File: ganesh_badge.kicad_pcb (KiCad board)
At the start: 2 copper layers, 36 x 47.8 mm, 14 parts, among them J1 Conn_01x03_Male, J2 USB_B_Micro, SW1 SW_Push, U1 ATtiny9-TS

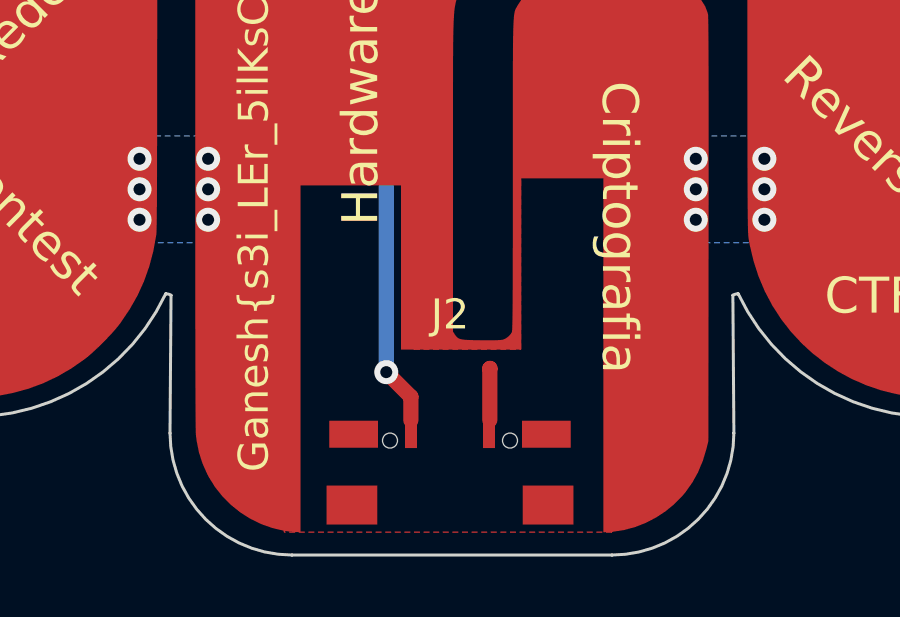
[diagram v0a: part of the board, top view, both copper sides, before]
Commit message: simple text fixes
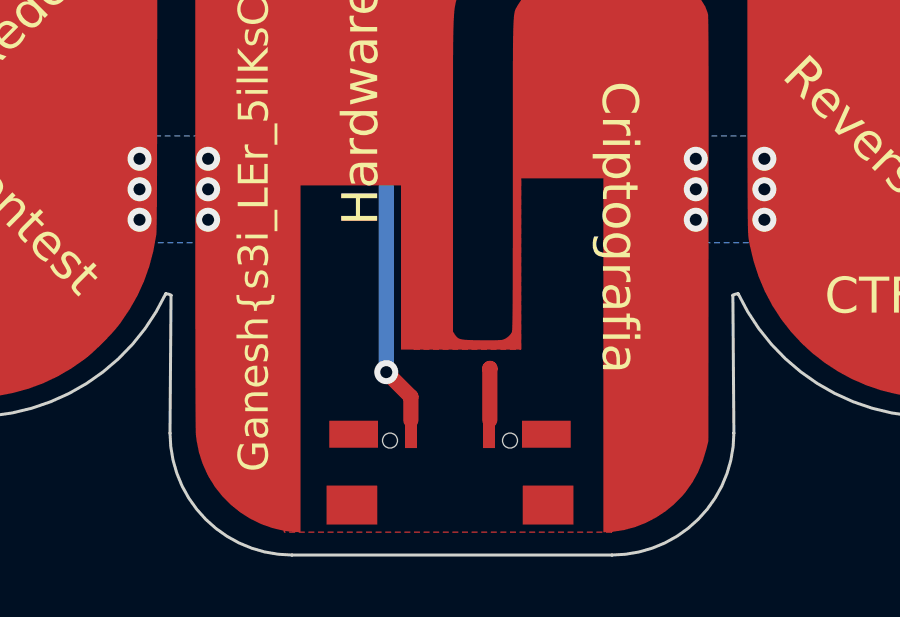
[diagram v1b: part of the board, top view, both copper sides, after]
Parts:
- C2: value 1.5 n -> 1.5 nF
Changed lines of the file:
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@@
     (property "Sheetname" "")
     (attr smd)
-    (fp_text reference "J2" (at 0 -7 unlocked) (layer "F.SilkS")
+    (fp_text reference "J2" (at 0 -7 unlocked) (layer "F.SilkS") hide
       (effects (font (size 1 1) (thickness 0.15)))
     )
@@
       (effects (font (size 1 1) (thickness 0.15)))
     )
-    (fp_text value "1.5 n" (at 2.084 0 180) (layer "F.Fab")
-      (effects (font (size 1 1) (thickness 0.15)))
-    )
+    (fp_text value "1.5 nF" (at 2.084 0 180) (layer "F.Fab")
+      (effects (font (size 1 1) (thickness 0.15)))
+    )

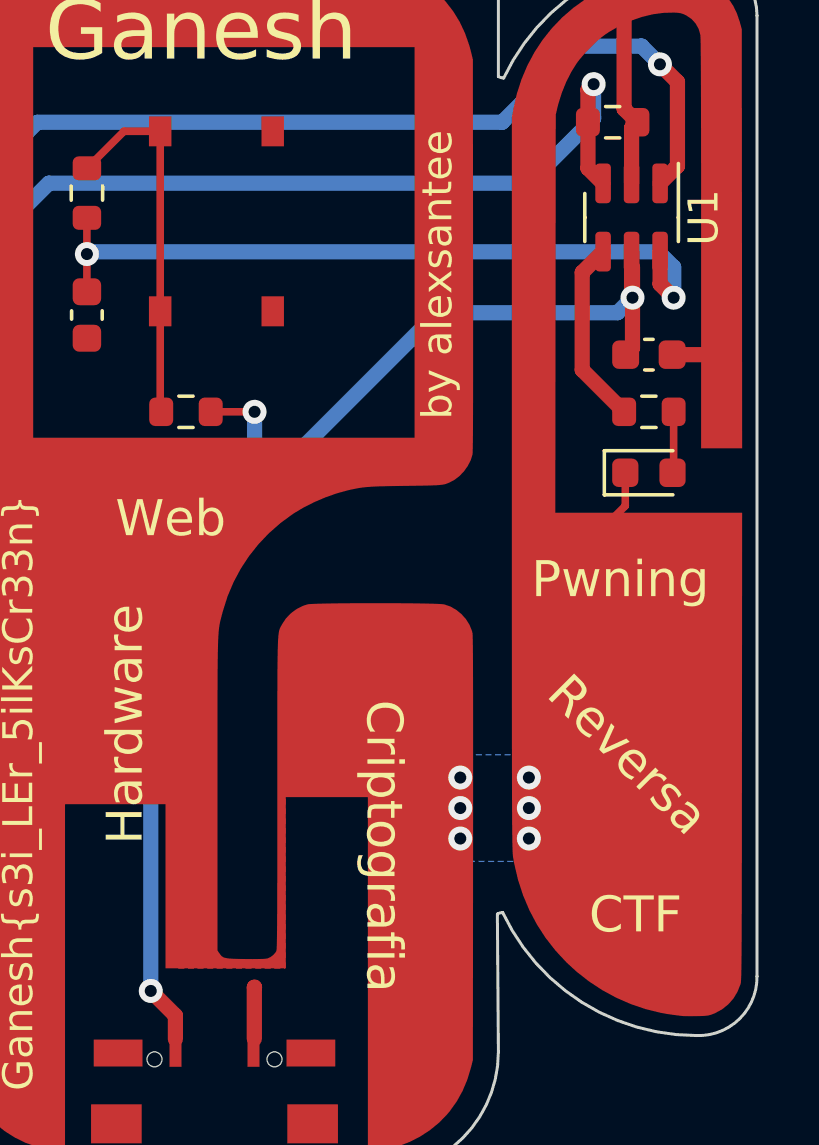
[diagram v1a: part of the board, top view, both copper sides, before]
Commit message: changes pic_version to main version and discards attiny
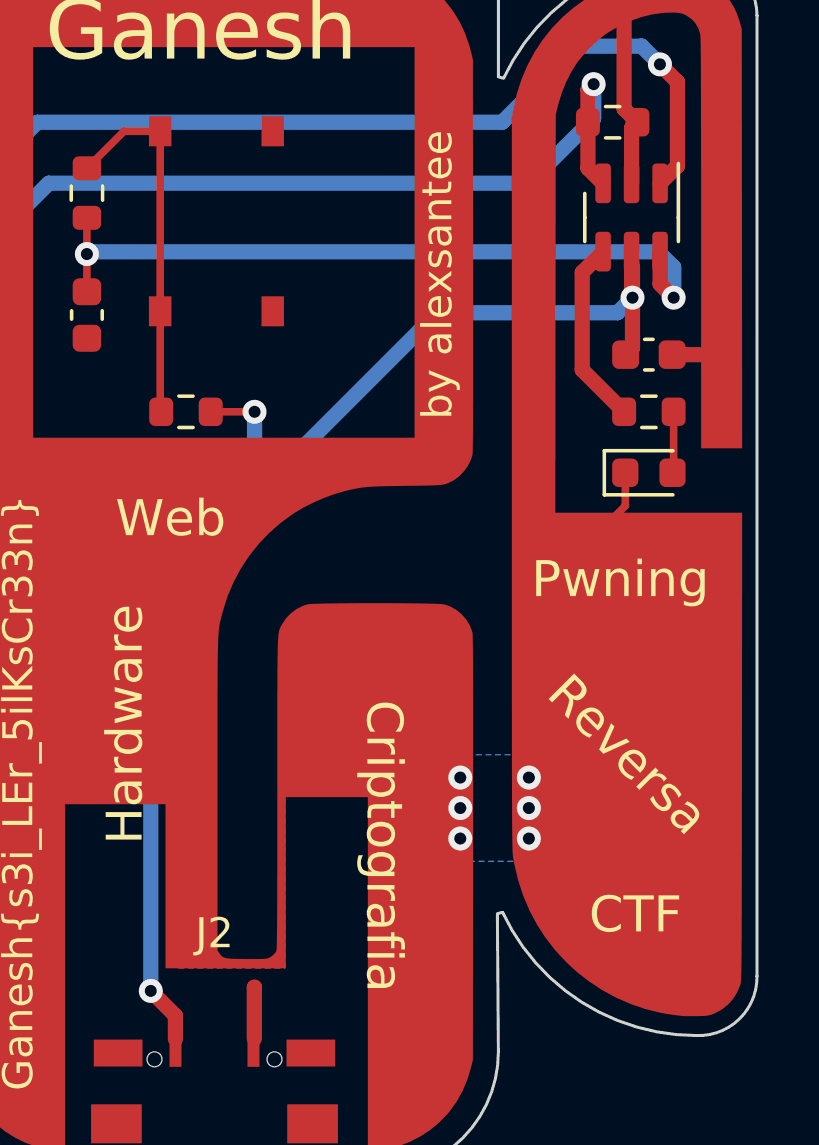
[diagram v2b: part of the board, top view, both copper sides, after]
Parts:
- C2: value 1.5 nF -> 1.5 n
- U1: value ATtiny9-TS -> PIC10F202T-I/OT
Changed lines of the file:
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@@
     (descr "LED SMD 0603 (1608 Metric), square (rectangular) end terminal, IPC_7351 nominal, (Body size source: http://www.tortai-tech.com/upload/download/2011102023233369053.pdf), generated with kicad-footprint-generator")
     (tags "LED")
-    (property "Sheetfile" "ganesh_badge.kicad_sch")
+    (property "Sheetfile" "File: ganesh_badge.kicad_sch")
     (property "Sheetname" "")
     (attr smd)
@@
     (descr "Resistor SMD 0603 (1608 Metric), square (rectangular) end terminal, IPC_7351 nominal, (Body size source: IPC-SM-782 page 72, https://www.pcb-3d.com/wordpress/wp-content/uploads/ipc-sm-782a_amendment_1_and_2.pdf), generated with kicad-footprint-generator")
     (tags "resistor")
-    (property "Sheetfile" "ganesh_badge.kicad_sch")
+    (property "Sheetfile" "File: ganesh_badge.kicad_sch")
     (property "Sheetname" "")
     (attr smd)
@@
     (descr "Resistor SMD 0603 (1608 Metric), square (rectangular) end terminal, IPC_7351 nominal, (Body size source: IPC-SM-782 page 72, https://www.pcb-3d.com/wordpress/wp-content/uploads/ipc-sm-782a_amendment_1_and_2.pdf), generated with kicad-footprint-generator")
     (tags "resistor")
-    (property "Sheetfile" "ganesh_badge.kicad_sch")
+    (property "Sheetfile" "File: ganesh_badge.kicad_sch")
     (property "Sheetname" "")
     (attr smd)
@@
   (footprint "Custom_Footprints:MicroQTJ_2pads" (layer "F.Cu")
     (at 52.259 71.12)
-    (property "Sheetfile" "ganesh_badge.kicad_sch")
-    (property "Sheetname" "")
-    (attr smd)
-    (fp_text reference "J2" (at 0 -7 unlocked) (layer "F.SilkS") hide
+    (property "Sheetfile" "File: ganesh_badge.kicad_sch")
+    (property "Sheetname" "")
+    (attr smd)
+    (fp_text reference "J2" (at 0 -7 unlocked) (layer "F.SilkS")
       (effects (font (size 1 1) (thickness 0.15)))
     )
@@
     (descr "Capacitor SMD 0603 (1608 Metric), square (rectangular) end terminal, IPC_7351 nominal, (Body size source: IPC-SM-782 page 76, https://www.pcb-3d.com/wordpress/wp-content/uploads/ipc-sm-782a_amendment_1_and_2.pdf), generated with kicad-footprint-generator")
     (tags "capacitor")
-    (property "Sheetfile" "ganesh_badge.kicad_sch")
+    (property "Sheetfile" "File: ganesh_badge.kicad_sch")
     (property "Sheetname" "")
     (attr smd)
@@
   (footprint "Custom_Footprints:TS-1187A-B-A-B" (layer "F.Cu")
     (at 52.324 40.386 90)
-    (property "Sheetfile" "ganesh_badge.kicad_sch")
+    (property "Sheetfile" "File: ganesh_badge.kicad_sch")
     (property "Sheetname" "")
     (attr smd)
@@
     (descr "Resistor SMD 0603 (1608 Metric), square (rectangular) end terminal, IPC_7351 nominal, (Body size source: IPC-SM-782 page 72, https://www.pcb-3d.com/wordpress/wp-content/uploads/ipc-sm-782a_amendment_1_and_2.pdf), generated with kicad-footprint-generator")
     (tags "resistor")
-    (property "Sheetfile" "ganesh_badge.kicad_sch")
+    (property "Sheetfile" "File: ganesh_badge.kicad_sch")
     (property "Sheetname" "")
     (attr smd)
@@
     (descr "Resistor SMD 0603 (1608 Metric), square (rectangular) end terminal, IPC_7351 nominal, (Body size source: IPC-SM-782 page 72, https://www.pcb-3d.com/wordpress/wp-content/uploads/ipc-sm-782a_amendment_1_and_2.pdf), generated with kicad-footprint-generator")
     (tags "resistor")
-    (property "Sheetfile" "ganesh_badge.kicad_sch")
+    (property "Sheetfile" "File: ganesh_badge.kicad_sch")
     (property "Sheetname" "")
     (attr smd)
@@
     (descr "SOT, 6 Pin (https://www.jedec.org/sites/default/files/docs/Mo-178c.PDF variant AB), generated with kicad-footprint-generator ipc_gullwing_generator.py")
     (tags "SOT TO_SOT_SMD")
-    (property "Sheetfile" "ganesh_badge.kicad_sch")
-    (property "Sheetname" "")
-    (attr smd)
-    (fp_text reference "U1" (at 0 -2.4 -90) (layer "F.SilkS")
-      (effects (font (size 1 1) (thickness 0.15)))
-    )
-    (fp_text value "ATtiny9-TS" (at 0 2.4 -90) (layer "F.Fab")
+    (property "Sheetfile" "File: ganesh_badge.kicad_sch")
+    (property "Sheetname" "")
+    (attr smd)
+    (fp_text reference "U1" (at 0 -2.4 -90) (layer "F.SilkS") hide
+      (effects (font (size 1 1) (thickness 0.15)))
+    )
+    (fp_text value "PIC10F202T-I/OT" (at 0 2.4 -90) (layer "F.Fab")
       (effects (font (size 1 1) (thickness 0.15)))
     )
@@
     (fp_line (start 0.8 1.45) (end -0.8 1.45) (layer "F.Fab") (width 0.1))
     (pad "1" smd roundrect (at -1.1375 -0.95 270) (size 1.325 0.52) (layers "F.Cu" "F.Paste" "F.Mask") (roundrect_rratio 0.25)
-      (net 4 "/tx") (pinfunction "PB0") (pintype "bidirectional"))
+      (net 4 "/tx") (pinfunction "GP0") (pintype "bidirectional"))
     (pad "2" smd roundrect (at -1.1375 0 270) (size 1.325 0.52) (layers "F.Cu" "F.Paste" "F.Mask") (roundrect_rratio 0.25)
-      (net 1 "GND") (pinfunction "GND") (pintype "power_in"))
+      (net 1 "GND") (pinfunction "VSS") (pintype "power_in"))
     (pad "3" smd roundrect (at -1.1375 0.95 270) (size 1.325 0.52) (layers "F.Cu" "F.Paste" "F.Mask") (roundrect_rratio 0.25)
-      (net 3 "/rx") (pinfunction "PB1") (pintype "bidirectional"))
+      (net 3 "/rx") (pinfunction "GP1") (pintype "bidirectional"))
     (pad "4" smd roundrect (at 1.1375 0.95 270) (size 1.325 0.52) (layers "F.Cu" "F.Paste" "F.Mask") (roundrect_rratio 0.25)
-      (net 8 "/led") (pinfunction "PB2") (pintype "bidirectional"))
+      (net 8 "/led") (pinfunction "GP2") (pintype "bidirectional"))
     (pad "5" smd roundrect (at 1.1375 0 270) (size 1.325 0.52) (layers "F.Cu" "F.Paste" "F.Mask") (roundrect_rratio 0.25)
-      (net 5 "VBUS") (pinfunction "VCC") (pintype "power_in"))
+      (net 5 "VBUS") (pinfunction "VDD") (pintype "power_in"))
     (pad "6" smd roundrect (at 1.1375 -0.95 270) (size 1.325 0.52) (layers "F.Cu" "F.Paste" "F.Mask") (roundrect_rratio 0.25)
-      (net 7 "/button_lpout") (pinfunction "~{RESET}/PB3") (pintype "bidirectional"))
+      (net 7 "/button_lpout") (pinfunction "GP3") (pintype "input"))
     (model "${KICAD6_3DMODEL_DIR}/Package_TO_SOT_SMD.3dshapes/SOT-23-6.wrl"
       (offset (xyz 0 0 0))
@@
     (descr "Through hole straight pin header, 1x03, 2.00mm pitch, single row")
     (tags "Through hole pin header THT 1x03 2.00mm single row")
-    (property "Sheetfile" "ganesh_badge.kicad_sch")
+    (property "Sheetfile" "File: ganesh_badge.kicad_sch")
     (property "Sheetname" "")
     (property "exclude_from_bom" "")
@@
     (descr "Capacitor SMD 0603 (1608 Metric), square (rectangular) end terminal, IPC_7351 nominal, (Body size source: IPC-SM-782 page 76, https://www.pcb-3d.com/wordpress/wp-content/uploads/ipc-sm-782a_amendment_1_and_2.pdf), generated with kicad-footprint-generator")
     (tags "capacitor")
-    (property "Sheetfile" "ganesh_badge.kicad_sch")
+    (property "Sheetfile" "File: ganesh_badge.kicad_sch")
     (property "Sheetname" "")
     (attr smd)
@@
       (effects (font (size 1 1) (thickness 0.15)))
     )
-    (fp_text value "1.5 nF" (at 2.084 0 180) (layer "F.Fab")
-      (effects (font (size 1 1) (thickness 0.15)))
-    )
+    (fp_text value "1.5 n" (at 2.084 0 180) (layer "F.Fab")
+      (effects (font (size 1 1) (thickness 0.15)))
+    )

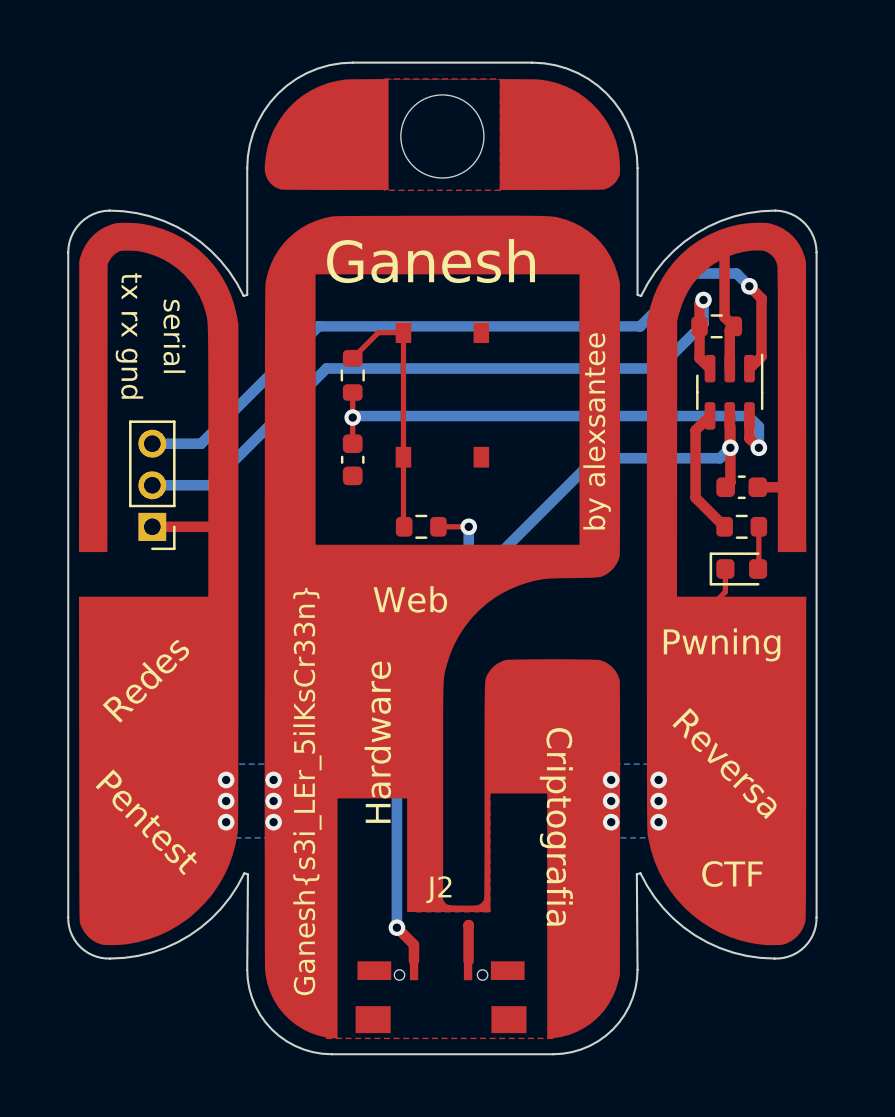
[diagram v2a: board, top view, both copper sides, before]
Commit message: changed header to be more compatible with pickit3
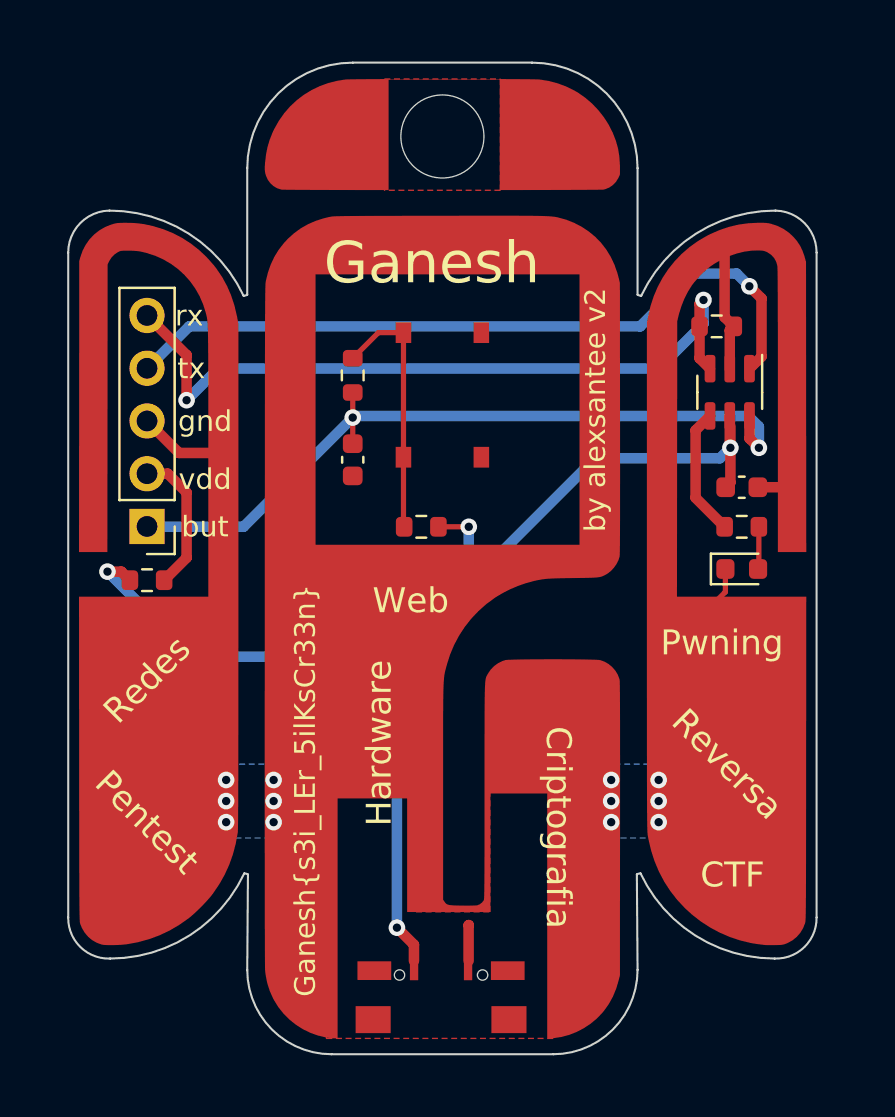
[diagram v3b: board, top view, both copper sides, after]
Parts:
- added R4: 250, Resistor_SMD:R_0603_1608Metric, F.Cu at (38.1, 49.3)
- J1: value Conn_01x03_Male -> Conn_01x05_Male; footprint Connector_PinHeader_2.00mm:PinHeader_1x03_P2.00mm_Vertical -> Connector_PinHeader_2.54mm:PinHeader_1x05_P2.54mm_Vertical
- U1: value PIC10F202T-I/OT -> ATtiny9-TS
- moved J1 0.25 mm to (38.1, 46.7)
- renumbered R2 to R1, R4 to R2, R1 to R5
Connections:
- J1 pad 1: GND -> /button_lpout
- J1 pad 2: /rx -> /header_vcc
- J1 pad 3: /tx -> GND
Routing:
- net VBUS: track 44.0 -> 60.9 mm, vias 3 -> 4
- net /button_lpout: track 25.0 -> 37.1 mm
- net /header_vcc: track 0.00 -> 6.95 mm
- net /rx: track 34.5 -> 36.0 mm, vias 1 -> 2
- net /tx: track 36.8 -> 35.6 mm
- net GND: track 15.3 -> 16.2 mm
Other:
- board text added: "but"
- board text added: "by alexsantee v2"
- board text added: "gnd"
- board text added: "rx"
- board text added: "tx"
- board text added: "vdd"
- board text removed: "by alexsantee"
- board text removed: "serial"
- board text removed: "tx rx gnd"
